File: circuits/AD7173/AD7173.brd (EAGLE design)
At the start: 21.4 x 31.2 mm, 37 parts, among them IC1 AD7173, IC2 ADP1720, IC3 ADP1720ARMZ-5, IC4 ADR445BR, Q1 FA-20H

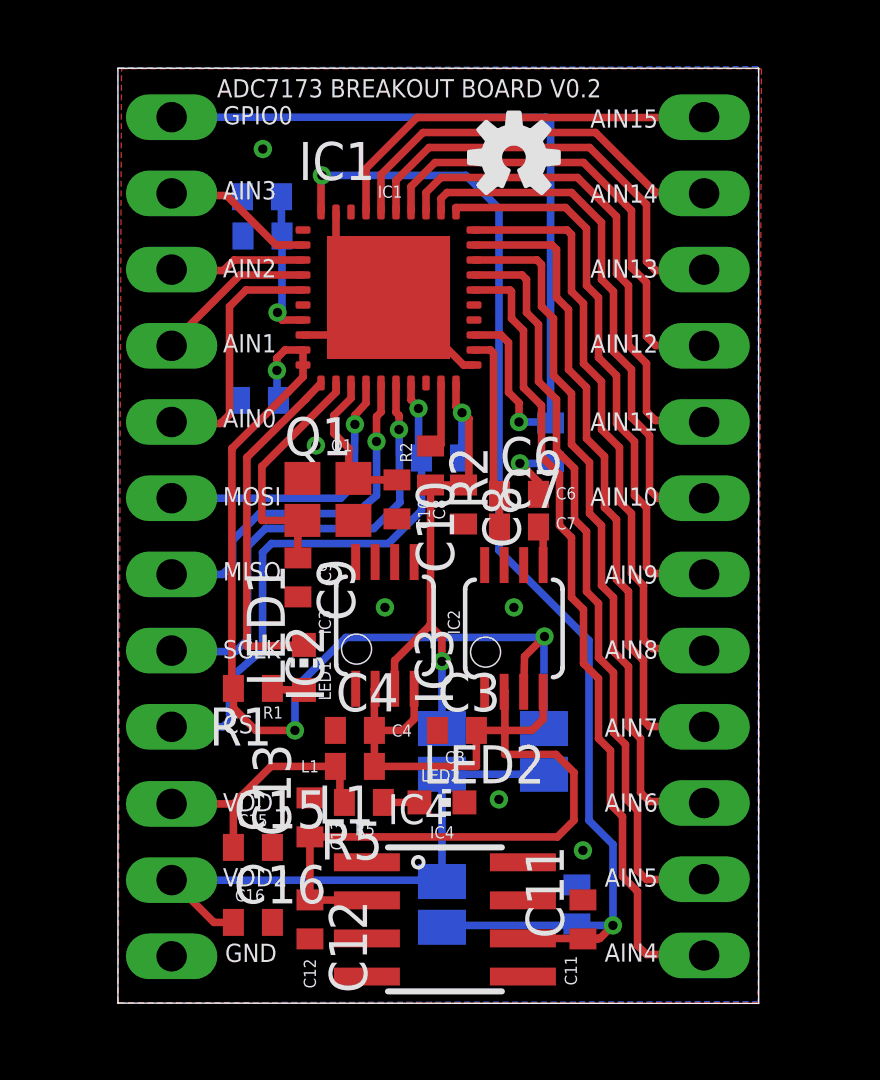
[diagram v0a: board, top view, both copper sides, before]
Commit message: updated pins, components placing
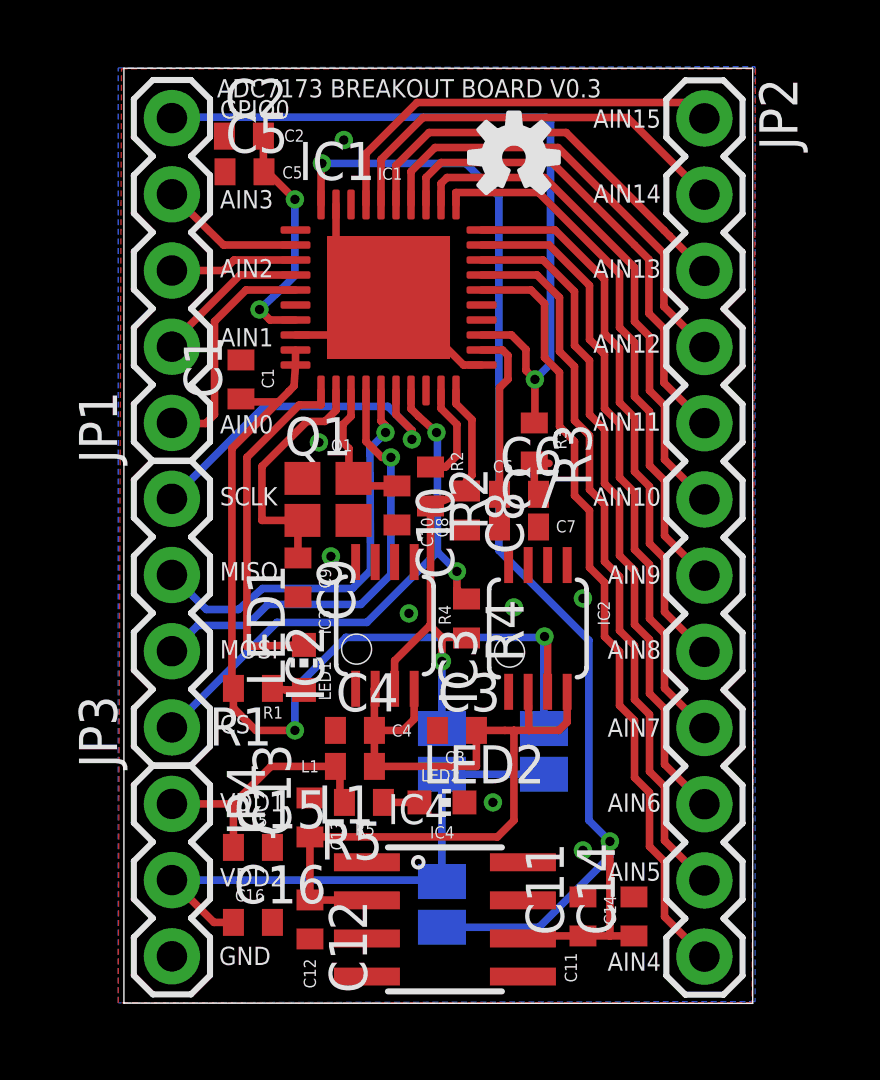
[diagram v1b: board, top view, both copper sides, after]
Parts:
- removed AIN0-3GPIO0: (no value), pinhead:1X05
- removed AIN4-15: (no value), pinhead:1X12
- removed POWER: (no value), pinhead:1X03
- removed SPI: (no value), pinhead:1X04
- added JP1: (no value), SparkFun-Connectors:1X05
- added JP2: (no value), SparkFun-Connectors:1X12
- added JP3: (no value), SparkFun-Connectors:1X04
- added JP4: (no value), SparkFun-Connectors:1X03
- moved R4 5.42 mm to (11.6, 12.8), flipped to the top, turned to 270 degrees
- moved C5 2.22 mm to (4.22, 27.7), flipped to the top, turned to 0 degrees
- moved C2 2.11 mm to (4.20, 28.9), flipped to the top, turned to 0 degrees
- moved C14 1.94 mm to (17.2, 2.90), flipped to the top
- moved C1 0.92 mm to (4.10, 20.8), flipped to the top, turned to 90 degrees
- moved IC3 0.80 mm to (14.0, 12.5)
- moved R2 0.70 mm to (10.4, 17.2)
- moved R3 0.54 mm to (13.9, 18.7), flipped to the top
- moved C8 0.22 mm to (11.6, 16.4)
- moved C10 0.20 mm to (9.30, 16.6)
- moved C11 0.10 mm to (15.5, 2.90)
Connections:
- net GND: now also JP4.3; no longer POWER.3
- net N$10: now also JP2.5; no longer AIN4-15.5
- net N$11: now also JP2.6; no longer AIN4-15.6
- net N$12: now also JP2.7; no longer AIN4-15.7
- net N$13: now also JP2.8; no longer AIN4-15.8
- net N$14: now also JP2.9; no longer AIN4-15.9
- net N$15: now also JP2.10; no longer AIN4-15.10
- net N$16: now also JP2.11; no longer AIN4-15.11
- net N$17: now also JP2.12; no longer AIN4-15.12
- net N$18: now also JP1.1; no longer AIN0-3GPIO0.1
- net N$19: now also JP1.2; no longer AIN0-3GPIO0.2
- net N$20: now also JP1.3; no longer AIN0-3GPIO0.3
- net N$21: now also JP1.4; no longer AIN0-3GPIO0.4
- net N$23: now also JP3.2; no longer SPI.4
- net N$24: now also JP3.3; no longer SPI.3
- net N$25: now also JP3.4; no longer SPI.2
- net N$28: now also JP4.2; no longer POWER.2
- net N$3: now also JP3.1; no longer SPI.1
- net N$30: now also JP4.1; no longer POWER.1
- net N$4: now also JP2.1; no longer AIN4-15.1
- net N$5: now also JP1.5; no longer AIN0-3GPIO0.5
- net N$7: now also JP2.2; no longer AIN4-15.2
- net N$8: now also JP2.3; no longer AIN4-15.3
- net N$9: now also JP2.4; no longer AIN4-15.4
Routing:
- net N$23: track 9.80 -> 15.0 mm
- net N$25: track 15.5 -> 11.8 mm
- net N$6: track 4.94 -> 8.13 mm, vias 1 -> 2
- net VIN: track 32.4 -> 29.2 mm
- net VCC: track 42.6 -> 44.9 mm
- net N$5: track 27.8 -> 25.7 mm
- net N$24: track 12.2 -> 13.9 mm
- net +5V: track 33.3 -> 31.9 mm, vias 3 -> 2
- net N$13: track 20.0 -> 18.6 mm
- net N$14: track 21.8 -> 20.5 mm
- net GND: track 14.4 -> 13.1 mm, vias 7 -> 8
- net N$15: track 23.5 -> 22.4 mm
- net +3V3: track 17.3 -> 16.2 mm, vias 2 -> 1
- net N$16: track 25.4 -> 24.3 mm
- net N$39: track 2.40 -> 3.43 mm
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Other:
- board size 21.4 x 31.2 mm -> 21 x 31.2 mm
- board text added: "ADC7173 BREAKOUT BOARD V0.3"
- board text removed: "ADC7173 BREAKOUT BOARD V0.2"

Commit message: small margin updates
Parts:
- moved R3 0.40 mm to (13.9, 19.1)
- moved C2 0.20 mm to (4.40, 28.9)
- moved C6 0.20 mm to (13.4, 17.2)
- moved C5 0.18 mm to (4.40, 27.7)
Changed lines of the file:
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@@
 <wire x1="0.2" y1="31.174" x2="0.2" y2="0.01" width="0" layer="20"/>
 <text x="5.2" y="20.5" size="0.4064" layer="121" font="vector" ratio="10" rot="R90">C1</text>
-<text x="6.211803125" y="29.1289875" size="0.4064" layer="121" font="vector" ratio="10" rot="R180">C2</text>
+<text x="6.311803125" y="29.1289875" size="0.4064" layer="121" font="vector" ratio="10" rot="R180">C2</text>
 <text x="10.9" y="8" size="0.4064" layer="121" font="vector" ratio="10">C3</text>
 <text x="9.8" y="9.3" size="0.4064" layer="121" font="vector" ratio="10" rot="R180">C4</text>
@@
 <text x="5.5" y="9.9" size="0.4064" layer="121" font="vector" ratio="10" rot="R180">R1</text>
 <text x="11.1" y="18.4" size="0.4064" layer="121" font="vector" ratio="10" rot="R270">R2</text>
-<text x="14.5481875" y="19.131803125" size="0.4064" layer="121" font="vector" ratio="10" rot="R270">R3</text>
+<text x="14.5481875" y="19.431803125" size="0.4064" layer="121" font="vector" ratio="10" rot="R270">R3</text>
 <text x="3.4" y="26.5" size="0.6096" layer="121" font="vector" ratio="10">AIN3</text>
 <text x="3.4" y="24.2" size="0.6096" layer="121" font="vector" ratio="10">AIN2</text>
@@
 <text x="18.1" y="27.3" size="0.6096" layer="121" font="vector" ratio="10" rot="R180">AIN14</text>
 <text x="18.1" y="29.8" size="0.6096" layer="121" font="vector" ratio="10" rot="R180">AIN15</text>
-<text x="12.5" y="17.7" size="0.4064" layer="121" font="vector" ratio="10">C6</text>
+<text x="12.5" y="17.9" size="0.4064" layer="121" font="vector" ratio="10">C6</text>
 <text x="14.6" y="15.7" size="0.4064" layer="121" font="vector" ratio="10">C7</text>
 <text x="10.6" y="16.2" size="0.4064" layer="121" font="vector" ratio="10" rot="R270">C8</text>
@@
 <text x="7.1" y="12.3" size="0.4064" layer="121" font="vector" ratio="10" rot="R90">IC3</text>
 <text x="16.4" y="12.6" size="0.4064" layer="121" font="vector" ratio="10" rot="R90">IC2</text>
-<text x="5.48" y="27.5" size="0.4064" layer="121" font="vector" ratio="10">C5</text>
+<text x="5.58" y="27.5" size="0.4064" layer="121" font="vector" ratio="10">C5</text>
 <text x="3.37" y="1.28" size="0.6096" layer="121" font="vector" ratio="10">GND</text>
 <text x="3.3" y="30.2" size="0.6096" layer="121" font="vector" ratio="10">ADC7173 BREAKOUT BOARD V0.3</text>
@@
 <element name="C1" library="rcl" package="C0402" value="0.1uF" x="4.1" y="20.8" rot="R90"/>
 <element name="R2" library="rcl" package="R0402" value="10k" x="10.42" y="17.23" rot="R270"/>
-<element name="R3" library="rcl" package="R0402" value="10k" x="13.88" y="18.7" rot="R270"/>
-<element name="C2" library="rcl" package="C0402" value="0.1uF" x="4.2" y="28.91"/>
+<element name="R3" library="rcl" package="R0402" value="10k" x="13.88" y="19.1" rot="R270"/>
+<element name="C2" library="rcl" package="C0402" value="0.1uF" x="4.4" y="28.9"/>
 <element name="C3" library="rcl" package="C0402" value="4.7uF" x="11.3" y="9.1"/>
-<element name="C5" library="rcl" package="C0402" value="1uF" x="4.22" y="27.72"/>
-<element name="C6" library="rcl" package="C0402" value="0.1uF" x="13.37" y="16.97"/>
+<element name="C5" library="rcl" package="C0402" value="1uF" x="4.4" y="27.7"/>
+<element name="C6" library="rcl" package="C0402" value="0.1uF" x="13.37" y="17.17"/>
 <element name="C7" library="rcl" package="C0402" value="1uF" x="13.37" y="15.88"/>
 <element name="C8" library="rcl" package="C0402" value="0.1uF" x="11.62" y="16.43" rot="R270"/>
@@
 <via x="12.5" y="6.7" extent="1-16" drill="0.31"/>
 <via x="15.5" y="13.5" extent="1-16" drill="0.31"/>
-<wire x1="14.37" y1="18" x2="13.88" y2="18.05" width="0.254" layer="1"/>
 <contactref element="C16" pad="2"/>
 <via x="15.5" y="5.1" extent="1-16" drill="0.31"/>
-<wire x1="14.02" y1="16.97" x2="13.88" y2="17.11" width="0.254" layer="1"/>
-<wire x1="13.88" y1="17.11" x2="13.88" y2="18.05" width="0.254" layer="1"/>
+<wire x1="14.02" y1="17.17" x2="13.88" y2="17.11" width="0.254" layer="1"/>
+<wire x1="13.88" y1="17.11" x2="13.88" y2="18.45" width="0.254" layer="1"/>
 <contactref element="JP4" pad="3"/>
 <via x="9.7" y="13" extent="1-16" drill="0.31"/>
@@
 <contactref element="R1" pad="2"/>
 <wire x1="5.92" y1="21.78" x2="5.92" y2="21.28" width="0.254" layer="1"/>
-<wire x1="5.92" y1="21.28" x2="5.87" y2="20.58" width="0.254" layer="1"/>
 <wire x1="5.87" y1="20.58" x2="5.7" y2="20.4" width="0.254" layer="1"/>
 <wire x1="5.7" y1="20.4" x2="5.35" y2="20.05" width="0.254" layer="1"/>
@@
 <wire x1="14.22" y1="12.23" x2="14.324" y2="12.126" width="0.254" layer="1"/>
 <wire x1="14.324" y1="12.126" x2="14.324" y2="10.387" width="0.254" layer="1"/>
+<wire x1="5.92" y1="21.28" x2="5.87" y2="21.28" width="0.254" layer="1"/>
+<wire x1="5.87" y1="21.28" x2="5.87" y2="20.58" width="0.254" layer="1"/>
 </signal>
 <signal name="N$3">
@@
 <wire x1="13.9" y1="20.8" x2="14.42" y2="21.32" width="0.254" layer="16"/>
 <wire x1="14.42" y1="21.32" x2="14.42" y2="29.38" width="0.254" layer="16"/>
-<wire x1="13.88" y1="19.35" x2="13.9" y2="19.47" width="0.254" layer="1"/>
+<wire x1="13.88" y1="19.75" x2="13.9" y2="19.47" width="0.254" layer="1"/>
 <wire x1="13.9" y1="19.47" x2="13.9" y2="20.8" width="0.254" layer="1"/>
 </signal>
@@
 <via x="5.9" y="26.8" extent="1-16" drill="0.31"/>
 <wire x1="5.9" y1="26.8" x2="4.98" y2="27.72" width="0.254" layer="1"/>
-<wire x1="4.98" y1="27.72" x2="4.87" y2="27.72" width="0.254" layer="1"/>
-<wire x1="4.87" y1="27.72" x2="4.85" y2="27.74" width="0.254" layer="1"/>
-<wire x1="4.85" y1="27.74" x2="4.85" y2="28.91" width="0.254" layer="1"/>
+<wire x1="4.98" y1="27.72" x2="5.05" y2="27.7" width="0.254" layer="1"/>
+<wire x1="5.05" y1="27.7" x2="5.05" y2="28.9" width="0.254" layer="1"/>
 </signal>
 <signal name="N$38">
@@
 <contactref element="IC1" pad="22"/>
 <wire x1="13" y1="20.8" x2="12.72" y2="20.52" width="0.254" layer="1"/>
-<wire x1="12.72" y1="20.52" x2="12.72" y2="16.97" width="0.254" layer="1"/>
-<wire x1="12.72" y1="16.97" x2="12.72" y2="15.88" width="0.254" layer="1"/>
+<wire x1="12.72" y1="20.52" x2="12.72" y2="17.17" width="0.254" layer="1"/>
+<wire x1="12.72" y1="17.17" x2="12.72" y2="15.88" width="0.254" layer="1"/>
 <wire x1="12.12" y1="21.78" x2="12.82" y2="21.78" width="0.254" layer="1"/>
 <wire x1="12.82" y1="21.78" x2="13" y2="21.6" width="0.254" layer="1"/>
